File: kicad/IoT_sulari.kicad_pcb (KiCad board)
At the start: 4 copper layers, 50.5 x 41 mm, 43 parts, among them J1 73412-0110, J2 73412-0110, J20 694106106102, J3 20021121-00010C4LF, J4 20021121-00010C4LF, J40 693043020611, SW1 SW_SPST, SW2 TL3301DF160QG, SW3 TL3301DF160QG, SW4 TL3301DF160QG, SW5 TL3301DF160QG, U2 NRF9160, U20 MIC5219-3.3YM5-TR, U40 TPD3F303DPVR

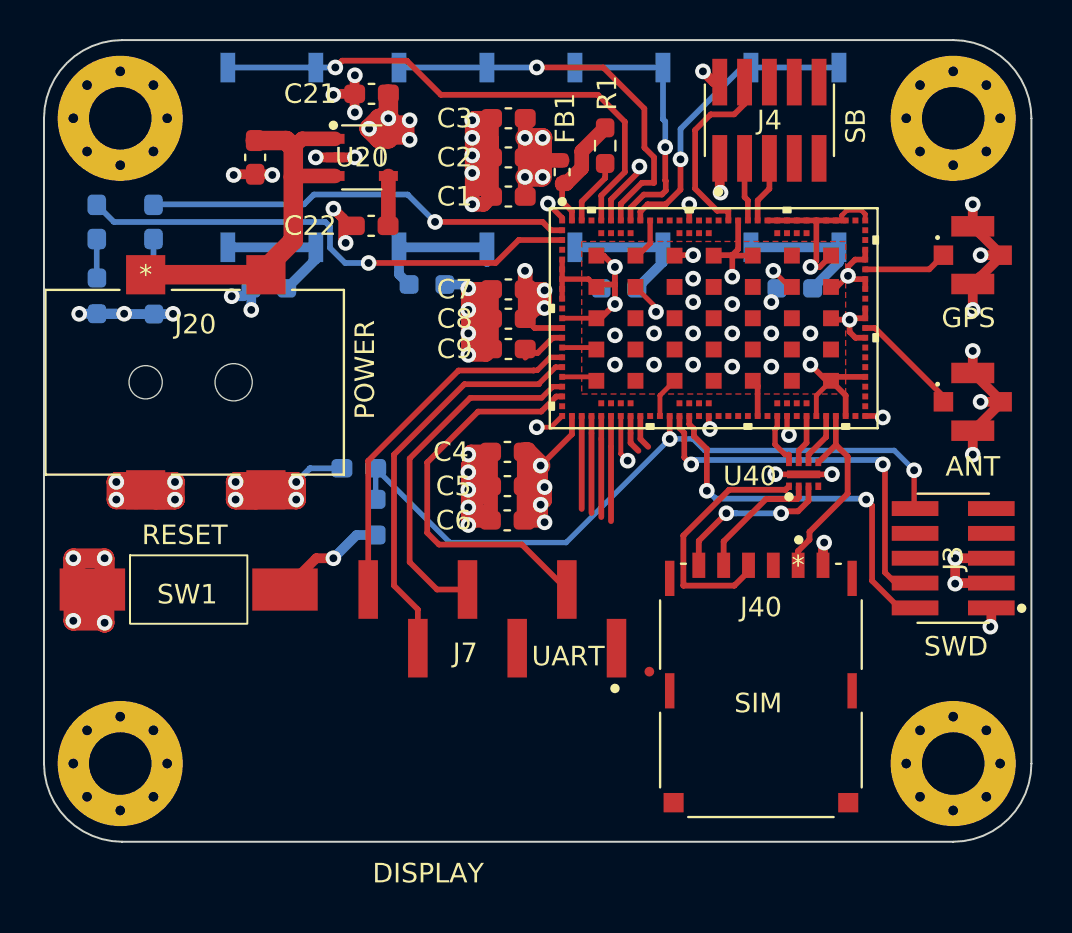
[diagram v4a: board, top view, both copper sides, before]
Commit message: changed Display connector
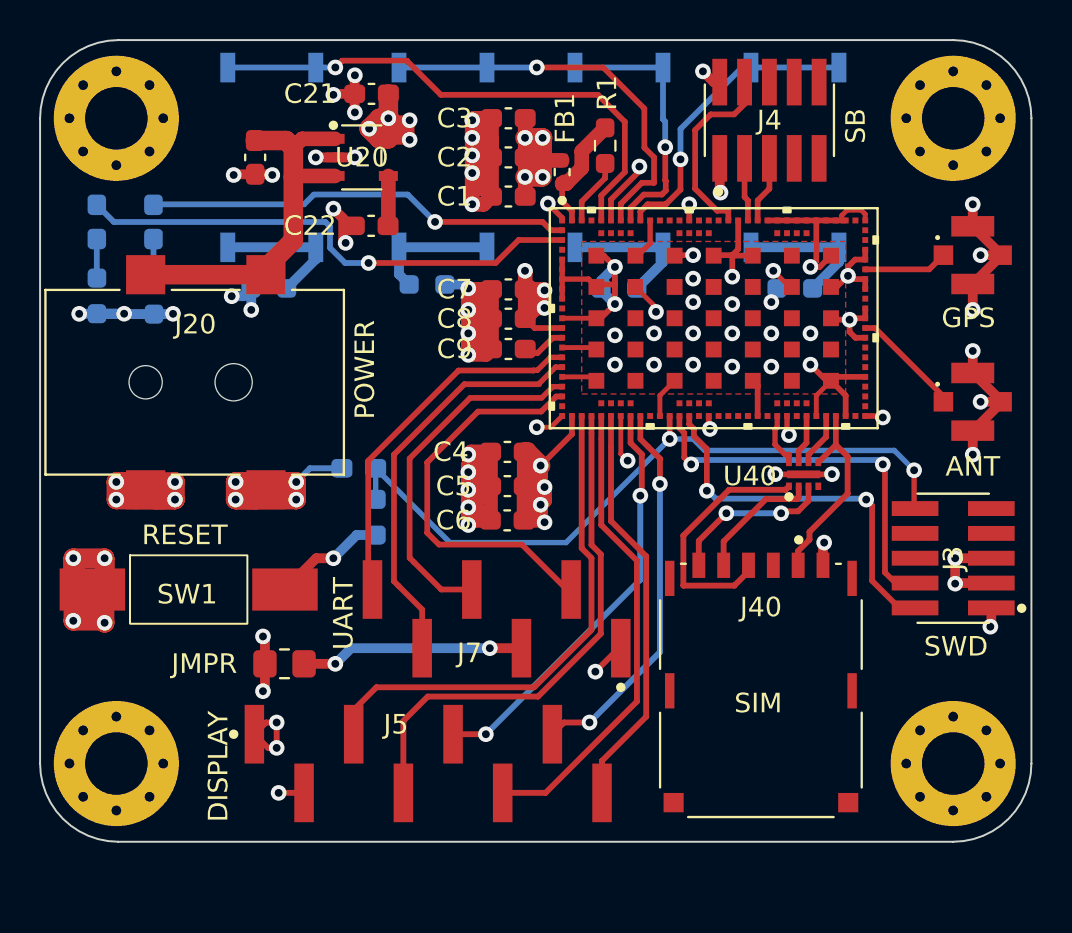
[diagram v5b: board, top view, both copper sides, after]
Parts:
- added J5: 10129380-908001ALF, 10129380-908001ALF:10129380-908001ALF, F.Cu at (112.2, 72.0)
- added JMPR: 0, Resistor_SMD:R_0805_2012Metric_Pad1.20x1.40mm_HandSolder, F.Cu at (104.8, 66.9)
- moved J7 0.22 mm to (115.7, 64.6)
- moved H1 0.20 mm to (96.2, 39.0)
- moved H4 0.20 mm to (96.2, 72.0)
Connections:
- J7 pad 3: +3.3V -> Net-(J7-Pad3)
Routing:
- net CLK: track 4.96 -> 27.0 mm
- net DIN: track 4.75 -> 26.2 mm
- net CS: track 1.95 -> 21.5 mm, vias 0 -> 2
- net DC: track 5.17 -> 24.2 mm
- net RST: track 1.74 -> 19.7 mm, vias 0 -> 2
- net BUSY: track 5.38 -> 21.0 mm
- net Net-(J7-Pad3): track 0.00 -> 11.5 mm, vias 0 -> 2
- net +3.3V: track 49.4 -> 56.4 mm, vias 17 -> 21
- net GND: track 223.5 -> 227.9 mm, vias 85 -> 87
- net Net-(R7-Pad2): track 7.38 -> 6.62 mm
- net Net-(U40-DATA2_OUT): track 9.05 -> 8.55 mm
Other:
- board size 50.5 x 41 mm -> 50.7 x 41 mm

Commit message: Edited copper fill zones, final touches
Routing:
- net GND: track 227.9 -> 156.9 mm
- net +3.3V: track 56.4 -> 15.0 mm, vias 21 -> 22
- added copper zone on F.Cu, net +3.3V

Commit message: Regenerate main board manufacturing files
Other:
- rule pad_to_mask_clearance: 0.05 -> 0
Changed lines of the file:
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@@
       (dielectric_constraints yes)
     )
-    (pad_to_mask_clearance 0.05)
+    (pad_to_mask_clearance 0)
     (pcbplotparams
       (layerselection 0x00010fc_ffffffff)
       (plot_on_all_layers_selection 0x0000000_00000000)
       (disableapertmacros false)
-      (usegerberextensions false)
+      (usegerberextensions true)
       (usegerberattributes true)
       (usegerberadvancedattributes true)
-      (creategerberjobfile true)
+      (creategerberjobfile false)
       (dashed_line_dash_ratio 12.000000)
       (dashed_line_gap_ratio 3.000000)
@@
       (psa4output false)
       (plotreference true)
-      (plotvalue true)
+      (plotvalue false)
       (plotinvisibletext false)
       (sketchpadsonfab false)
-      (subtractmaskfromsilk false)
+      (subtractmaskfromsilk true)
       (outputformat 1)
       (mirror false)
-      (drillshape 1)
+      (drillshape 0)
       (scaleselection 1)
-      (outputdirectory "")
+      (outputdirectory "gerber/")
     )
   )
@@
     (fp_line (start 1 0.625) (end -1 0.625)
       (stroke (width 0.1) (type solid)) (layer "F.Fab"))
-    (pad "1" smd roundrect (at -1 0) (size 1.2 1.4) (layers "F.Cu" "F.Paste" "F.Mask") (roundrect_rratio 0.208333)
+    (pad "1" smd roundrect (at -1 0) (size 1.2 1.4) (layers "F.Cu" "F.Paste" "F.Mask") (roundrect_rratio 0.2083333333)
       (net 13 "+3.3V") (pintype "passive"))
-    (pad "2" smd roundrect (at 1 0) (size 1.2 1.4) (layers "F.Cu" "F.Paste" "F.Mask") (roundrect_rratio 0.208333)
+    (pad "2" smd roundrect (at 1 0) (size 1.2 1.4) (layers "F.Cu" "F.Paste" "F.Mask") (roundrect_rratio 0.2083333333)
       (net 110 "Net-(J7-Pad3)") (pintype "passive"))
     (model "${KICAD6_3DMODEL_DIR}/Resistor_SMD.3dshapes/R_0805_2012Metric.wrl"
